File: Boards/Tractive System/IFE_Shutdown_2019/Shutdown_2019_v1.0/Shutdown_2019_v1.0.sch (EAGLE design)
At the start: 109 parts, among them Q1 DMN6140L-7, Q11 DMP3099L-7, Q12 IRLML6346PBF, Q13 IRLML6346PBF, Q14 IRLML6346PBF, Q15 DMP3099L-7, Q16 DMN6140L-7, Q17 IRLML6346PBF, Q2 DMN6140L-7, Q3 DMN6140L-7, Q4 DMN6140L-7, Q5 DMN6140L-7, Q6 DMP3099L-7, Q7 DMN6140L-7, Q8 DMN6140L-7, Q9 DMN6140L-7, U1 STM32F103CBT6

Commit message: starting to connect subsystems
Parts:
- removed R23: 4.7k, rcl:R-US_R0603
- U$11: value MCP2551 -> MCP2562; device Microchip_By_element14_Batch_1:MCP2551-I/SN -> MICROCHIP:MCP2562
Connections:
- removed net N$18: R23.1, U$11.RS
- removed net RXCAN: U$11.RXD
- removed net SWDCLK: JP1.4
- removed net TXCAN: U$11.TXD
- new net CAN_RX: U$11.RX, U1.PB8
- new net CAN_SBTY: U1.PB7
- new net CAN_STBY: U$11.STBY
- new net CAN_TX: U$11.TX, U1.PB9
- new net SPI1_MISO: U1.PA6
- new net SPI1_MOSI: U1.PA7
- new net SPI1_NSS: U1.PA4
- new net SPI1_SCK: U1.PA5
- new net SWCLK: JP1.4, U1.PA14
- net +3V3: now also U$11.VIO
- net FAULT_BMS_STATUS_3_3: now also U1.PA2
- net FAULT_BSPD_STATUS_3_3: now also U1.PA1
- net FAULT_IMD_STATUS_3_3: now also U1.PA3
- net GND: no longer R23.2
- net SWDIO: now also U1.PA13
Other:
- moved on the sheet: R19, R20

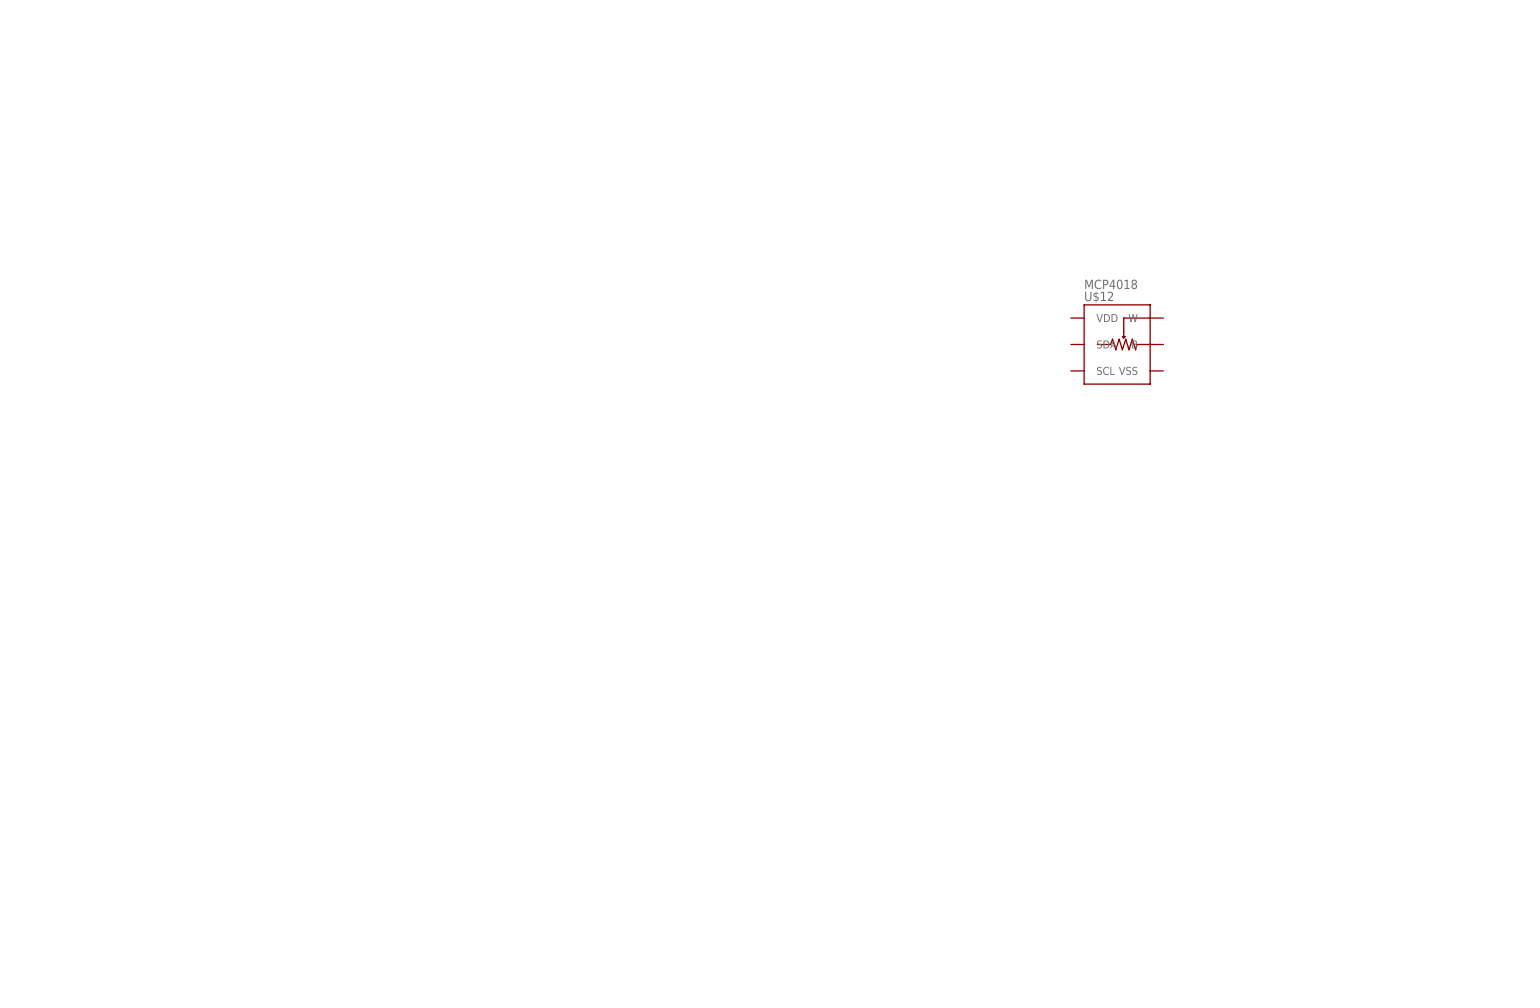
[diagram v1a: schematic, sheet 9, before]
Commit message: Added traction control mucrocontroller
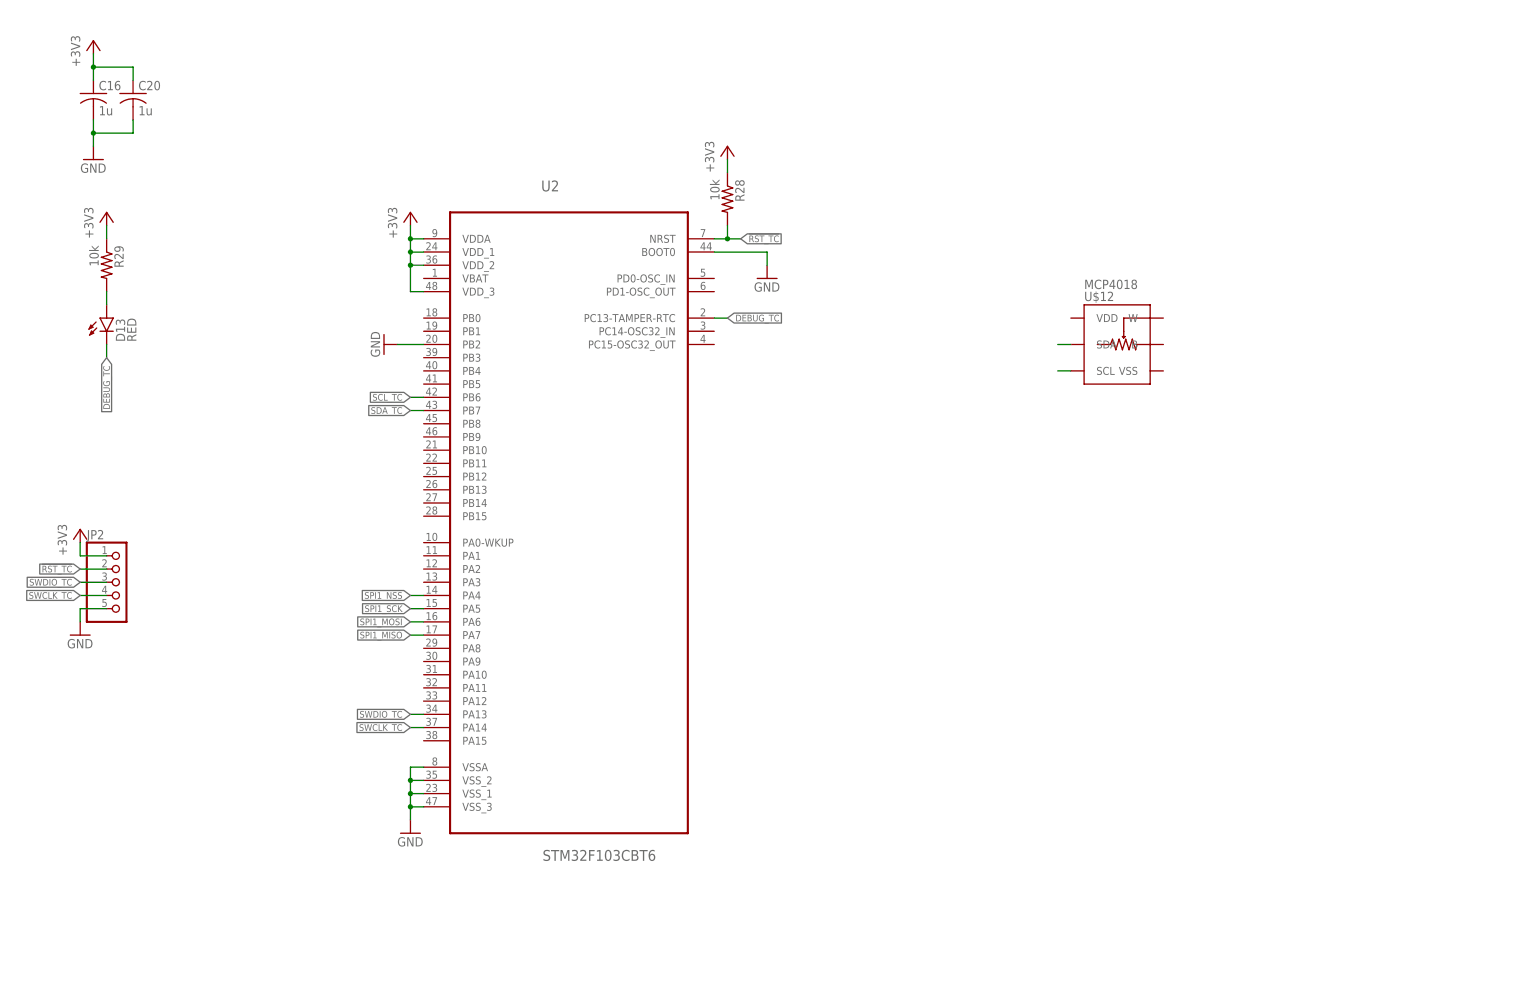
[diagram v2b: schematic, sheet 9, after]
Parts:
- added C16, C20: 1u, rcl:C-USC0805
- added D13: RED, SparkFun-LED:LED-RED0603
- added JP2: (no value), Headers_IFE:PINHD-1X5
- added Q10: DMN6140L-7, TRANS:DMN6140L-7
- added R23: 10k, resistor:R-US_R0603
- added R28, R29: 10k, rcl:R-US_R0603
- added U2: STM32F103CBT6, ST Microelctronics_By_element14_Batch_1:STM32F103CBT6
- R9: value (none) -> 1k
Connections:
- new net !RST_TC: JP2.2, R28.2, U2.NRST
- new net BRAKE_PRESSURE_3_3: U1.PB1
- new net DEBUG_TC: D13.C, U2.PC13-TAMPER-RTC
- new net HV_CONNECTED_3_3: Q10.D, R23.1, U1.PB10
- new net I2C1_SCL: U1.PB6
- new net I2C1_SDA: U1.PB7
- new net N$18: U1.PA9
- new net N$20: U1.PB14
- new net N$21: D13.A, R29.2
- new net N$22: U$12.SDA
- new net N$23: U$12.SCL
- new net N$5: U1.PA8
- new net REGEN_3_3: U1.PA0-WKUP
- new net SCL_TC: U2.PB6
- new net SDA_TC: U2.PB7
- new net SWCLK_TC: JP2.4, U2.PA14
- new net SWDIO_TC: JP2.3, U2.PA13
- new net THROTTLE_3_3: U1.PB0
- net +3V3: now also C16.1, C20.1, JP2.1, R23.2, R28.1, R29.1, U2.VDDA, U2.VDD_1, U2.VDD_2, U2.VDD_3
- net BRAKE_LIGHT_EN: now also U1.PB13
- net CAN_RX: now also U1.PA11; no longer U1.PB8
- net CAN_SBTY: now also U1.PA10; no longer U1.PB7
- net CAN_TX: now also U1.PA12; no longer U1.PB9
- net GND: now also C16.2, C20.2, JP2.5, Q10.S, U2.BOOT0, U2.PB2, U2.VSSA, U2.VSS_1, U2.VSS_2, U2.VSS_3
- net HV_CONNECTED: now also Q10.G
- net SPI1_MISO: now also U2.PA7
- net SPI1_MOSI: now also U2.PA6
- net SPI1_NSS: now also U2.PA4
- net SPI1_SCK: now also U2.PA5
- net TSAL_HV_EN: now also U1.PB11
- net TSAL_LV_EN: now also U1.PB12
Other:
- moved on the sheet: JP1

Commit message: Rework Enable
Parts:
- removed D3, D5, D6: 1N914, Diodes:1N914
- removed Q4, Q7, Q8: DMN6140L-7, TRANS:DMN6140L-7
- removed R2, R4, R7: 10k, rcl:R-US_R0603
- removed R_APPS, R_BTSF, R_RTD: PCN-112D3MHZ, Display_Custom:PCN-112D3MHZ
- removed R_BMS, R_BSPD, R_IMD: RT424012, Display_Custom:RT424012
- added Q18, Q20, Q21: DMN6140L-7, TRANS:DMN6140L-7
- added R30, R31, R32: 10k, rcl:R-US_R0603
- added U$13, U$14, U$15: EC2, KEMET:EC2
- C2, C8, C9: value 47u -> 10uF; device rcl:CPOL-USE2.5-7 -> rcl:C-USC0805
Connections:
- net THROTTLE_3_3 renamed THROTTLE_A_3_3
- removed net N$10: D5.A, Q7.D, R_BTSF.2
- removed net N$11: D6.A, Q8.D, R_RTD.2
- removed net N$12: R_BTSF.3, R_RTD.4
- removed net N$13: R_APPS.3, R_BTSF.4
- removed net N$20: U1.PB14
- removed net N$7: D3.A, Q4.D, R_APPS.2
- new net HALL_FL_3_3: U2.PB12
- new net HALL_FR_3_3: U2.PB13
- new net HALL_RL_3_3: U2.PB14
- new net HALL_RR_3_3: U2.PB15
- new net N$24: Q18.D, Q20.S
- new net N$25: Q18.S, Q21.D
- new net RTDS_EN: U1.PB3
- new net THROTTLE_B_3_3: U1.PB1
- net +12V: now also U$13.$P5, U$14.$P5, U$15.$P5; no longer D3.C, D5.C, D6.C, R_APPS.1, R_BMS.2_ACTIVE, R_BSPD.2_ACTIVE, R_BTSF.1, R_IMD.2_ACTIVE, R_RTD.1
- net AIR_IN: now also U$13.$P9; no longer R_BSPD.1_CENTER
- net AIR_OUT: now also U$15.$P8; no longer R_IMD.1_ACTIVE
- net APPS_EN: now also Q20.G, R30.2, U1.PB4; no longer Q4.G, R2.2
- net BRAKE_PRESSURE_3_3: now also U1.PA0-WKUP; no longer U1.PB1
- net BTSF_EN: now also Q18.G, R31.2, U1.PB5; no longer Q7.G, R4.2
- net ENABLE_IN: now also Q21.S; no longer R_APPS.4
- net ENABLE_OUT: now also Q20.D; no longer R_RTD.3
- net FAULT_BMS_STAT: now also C8.1, U$14.$P1, U$14.$P4; no longer C8.+, R_BMS.2_CENTER, R_BMS.COIL+
- net FAULT_BSPD_STAT: now also C2.1, U$13.$P1, U$13.$P4; no longer C2.+, R_BSPD.2_CENTER, R_BSPD.COIL+
- net FAULT_BSPD_STATUS_3_3: now also U1.PB14; no longer U1.PA1
- net FAULT_IMD_STAT: now also C9.1, U$15.$P1, U$15.$P4; no longer C9.+, R_IMD.2_CENTER, R_IMD.COIL+
- net GND: now also C2.2, C8.2, C9.2, R30.1, R31.1, R32.1; no longer C2.-, C8.-, C9.-, Q4.S, Q7.S, Q8.S, R2.1, R4.1, R7.1
- net N$1: now also U$14.$P12; no longer R_BMS.COIL-
- net N$27: now also U$13.$P8, U$14.$P9; no longer R_BMS.1_CENTER, R_BSPD.1_ACTIVE
- net N$28: now also U$13.$P3; no longer R_BSPD.2_REST
- net N$31: now also U$14.$P8, U$15.$P9; no longer R_BMS.1_ACTIVE, R_IMD.1_CENTER
- net N$32: now also U$13.$P12; no longer R_BSPD.COIL-
- net N$35: now also U$14.$P3; no longer R_BMS.2_REST
- net N$43: now also U$15.$P3; no longer R_IMD.2_REST
- net N$44: now also U$15.$P12; no longer R_IMD.COIL-
- net REGEN_3_3: now also U1.PA1; no longer U1.PA0-WKUP
- net RTD_EN: now also Q21.G, R32.2, U1.PB8; no longer Q8.G, R7.2

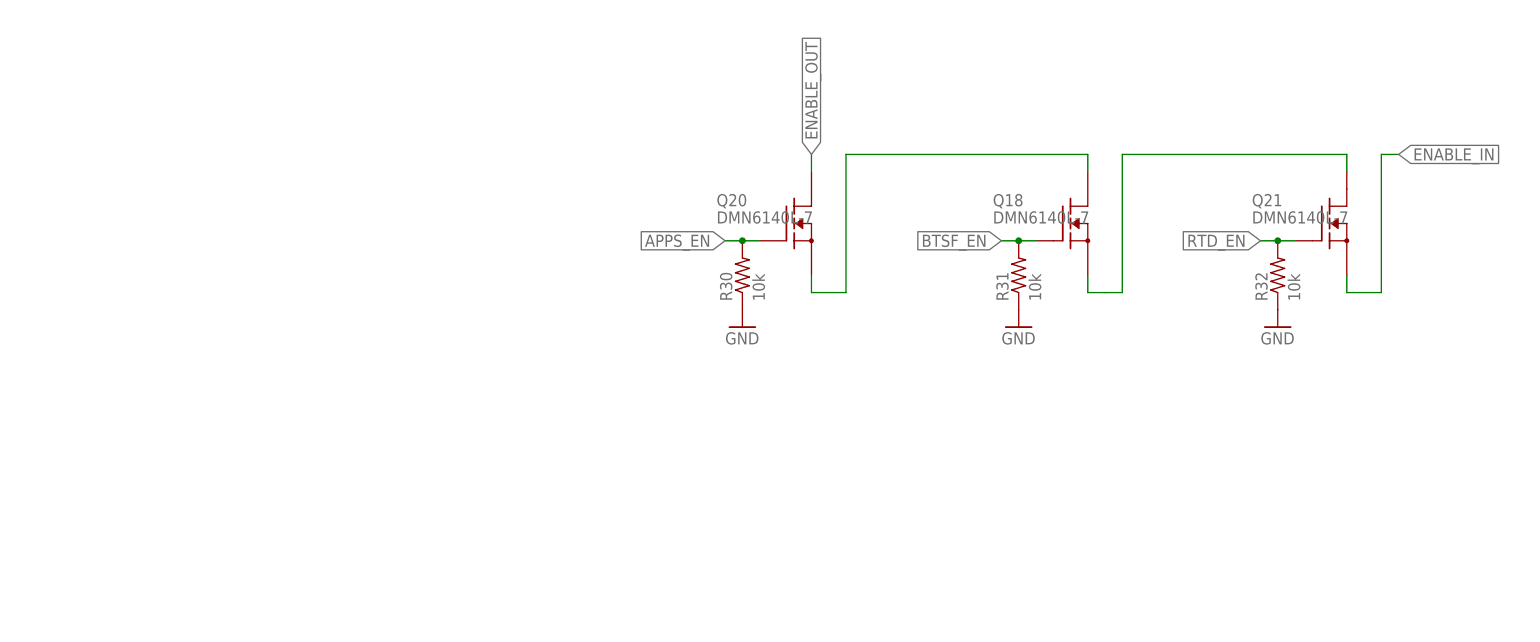
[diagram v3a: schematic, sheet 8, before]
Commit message: created op amp buffer
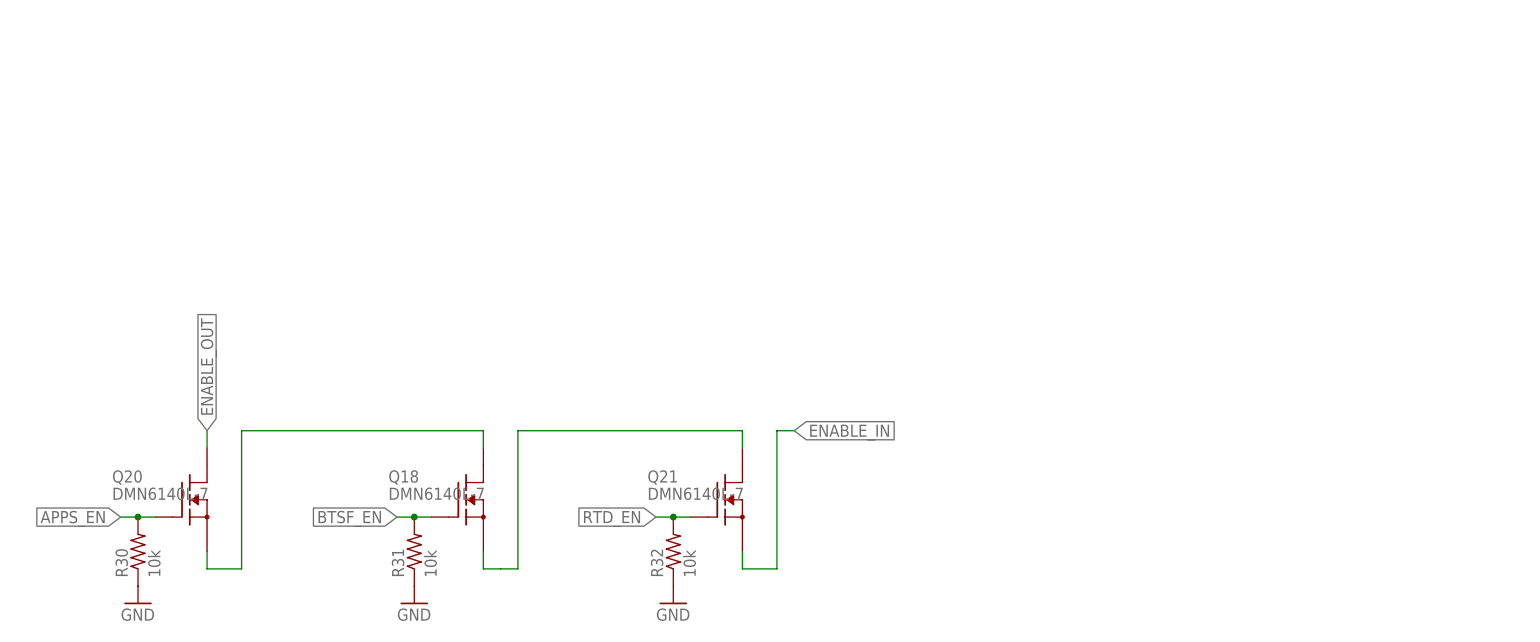
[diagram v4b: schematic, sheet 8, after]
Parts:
- removed BRAKE1, THROTTLE1: RTRIM3249W, Resistors:RTRIM3249W
- added C21: (no value), rcl:C-USC0603
- added CURRENT_SENSOR_SUPPLY1: MINIFIT_JR_5566-02, Display_Custom:MINIFIT_JR_5566-02
- added Q4: DMN6140L-7, TRANS:DMN6140L-7
- added R2, R4: (no value), rcl:R-US_R0603
- added R7: 50k, rcl:R-US_R0603
- added U$16, U$17: PV36, BOURNS:PV36
- added U$18: LMV321L, STM:LMV321L
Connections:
- removed net RESET: U$5.4
- new net N$10: D12.C, R4.2
- new net N$11: D11.C, R2.2
- new net N$12: R7.2, U$12.B, U$18.+IN
- new net N$20: U$12.W
- new net N$7: Q4.D
- net +3V3: now also D11.A
- net +5V: now also C21.1, CURRENT_SENSOR_SUPPLY1.1, D12.A, U$12.VDD, U$16.A, U$17.A, U$18.VDD; no longer BRAKE1.A, THROTTLE1.A
- net BRAKE_TH: now also U$16.W; no longer BRAKE1.S
- net FAULT_RESET: now also U$5.4
- net GND: now also C21.2, Q4.S, R2.1, R4.1, R7.1, U$12.VSS, U$16.B, U$17.B, U$18.GND; no longer BRAKE1.E, THROTTLE1.E
- net HV_CONNECTED: now also CURRENT_SENSOR_SUPPLY1.2; no longer U$5.2
- net RTDS_EN: now also Q4.G
- net THROTTLE_OUT: now also U$18.-IN, U$18.OUT
- net THROTTLE_TH: now also U$17.W; no longer THROTTLE1.S
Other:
- moved on the sheet: D11, D12, Q18, Q20, Q21, R30, R31, R32
